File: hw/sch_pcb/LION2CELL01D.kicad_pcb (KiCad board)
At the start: 2 copper layers, 80.8 x 60.5 mm, 100 parts, among them J1 JUMP_4X2, J10 JUMP_2x1, J11 JUMP_2x1, J12 JUMP_2x1, J13 JUMP_4X2, J14 JUMP_2x1, J15 CONN_2, J2 JUMP_2x1, J3 JUMP_2x1, J4 JUMP2_2x1, J5 JUMP_2x1, J6 JUMP_2x1, J7 JUMP_4X2, J8 CONN1_1, J9 CONN1_1, P1 _, P2 _, P3 _, P4 _, Q1 IRLML6244, SW1 SW_PUSH, U1 BQ29209, U2 BQ24103, U3 BQ34Z100, U4 SN74HC164D, U5 TPS76601, U6 APX810-31SAG-7

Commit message: Documentation update.
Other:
- net class Default removed
- net class Low_power removed

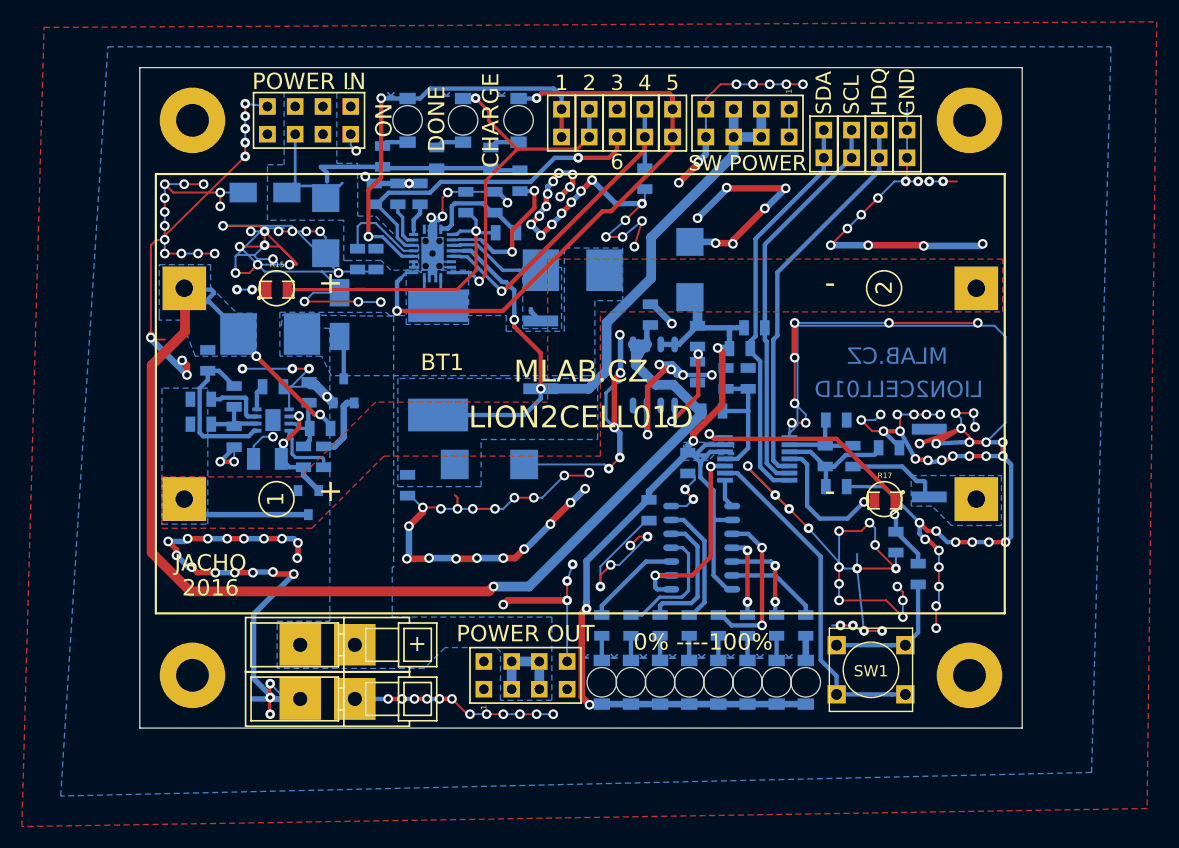
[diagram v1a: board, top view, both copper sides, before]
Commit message: Update documentation. Improve schematic (title block, texts) Regenerate PDF export.
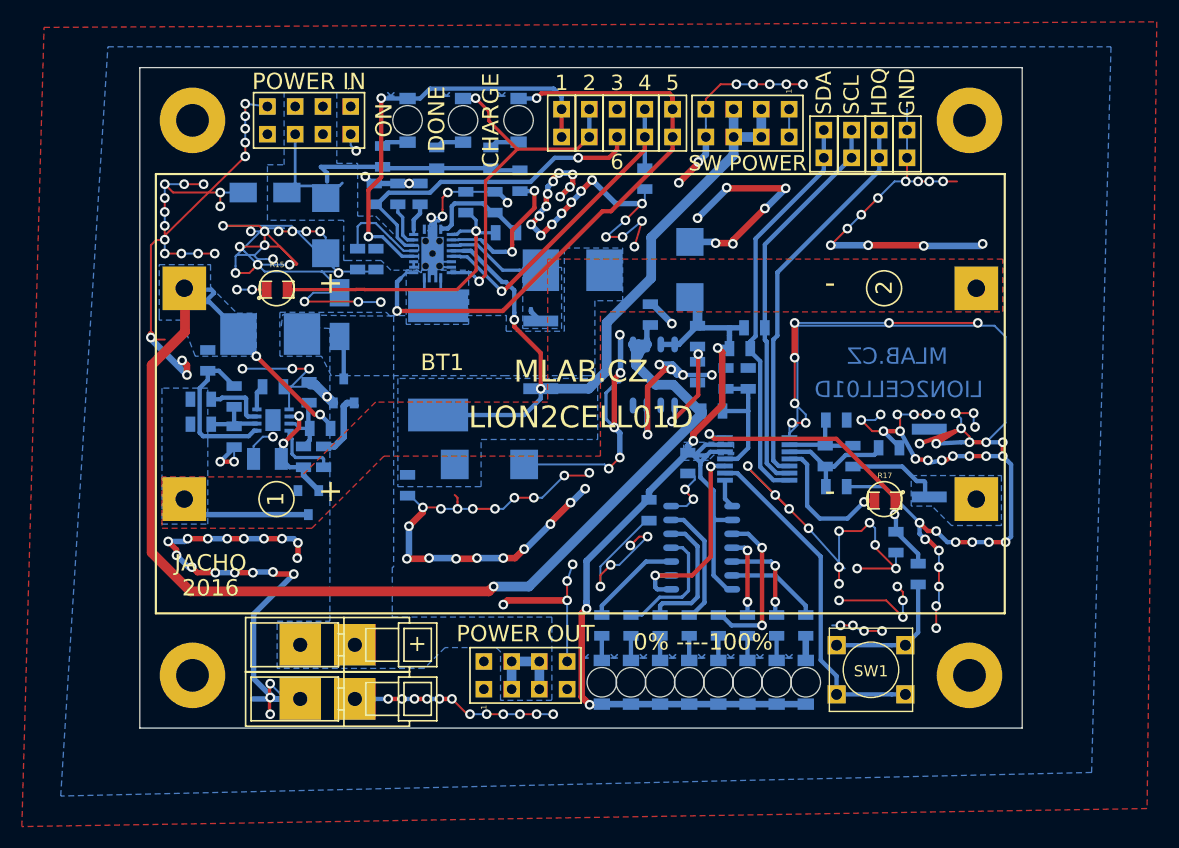
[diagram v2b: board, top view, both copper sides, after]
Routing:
- net GND: track 735.8 -> 726.1 mm
